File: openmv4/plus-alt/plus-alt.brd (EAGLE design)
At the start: 35.6 x 44.5 mm, 80 parts, among them M1 9774030243R, M2 9774030243R, Q1 BSS138, Q2 AO3401, U1 W25Q256JVEIQ_TR, U2 *, U3 ME6211C33M5G, U4 PAM2305AABADJ, U5 USBLC6-2, X1 MF-CON-MICROUSB-RIGHT, X2 USD-1040310811, X3 DF12-36-DS, X4 S2B-PH-K-S(LF)(SN), Y1 12M

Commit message: PureEngineering Updates
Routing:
- net VCC: track 125.5 -> 127.7 mm
- net VBUS: track 37.8 -> 39.8 mm
- net N$17: track 22.3 -> 23.7 mm
- net SPI2_NSS: track 16.7 -> 15.9 mm
- added copper zone on layer 5, net VCC
- removed copper zone on layer 16, net VBUS
- removed copper zone on layer 15, net VCC
- removed copper zone on layer 16, net VCC
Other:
- outline, holes or cut-outs redrawn

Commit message: Signals must be redone
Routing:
- net GND: track 136.2 -> 0.00 mm, vias 77 -> 0
- net VCC: track 127.7 -> 0.00 mm, vias 48 -> 0
- net SPI3_SCLK/TRACESWO: track 40.2 -> 0.00 mm, vias 3 -> 0
- net VBUS: track 39.8 -> 0.00 mm, vias 9 -> 0
- net SDIO_D0: track 36.9 -> 0.00 mm, vias 3 -> 0
- net DCMI_FSIN: track 36.8 -> 0.00 mm, vias 2 -> 0
- net DRAM_CLKE: track 35.2 -> 0.00 mm, vias 2 -> 0
- net DAC: track 34.6 -> 0.00 mm, vias 1 -> 0
- net SDIO_D1: track 34.3 -> 0.00 mm, vias 3 -> 0
- net TIM4_CH1: track 33.8 -> 0.00 mm, vias 1 -> 0
- net DRAM_DQM1: track 33.6 -> 0.00 mm, vias 1 -> 0
- net DRAM_D29: track 32.5 -> 0.00 mm, vias 2 -> 0
- net DCMI_RST: track 32.4 -> 0.00 mm, vias 4 -> 0
- net DRAM_D28: track 32.3 -> 0.00 mm, vias 2 -> 0
- net I2C1_SCL: track 31.6 -> 0.00 mm, vias 3 -> 0
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
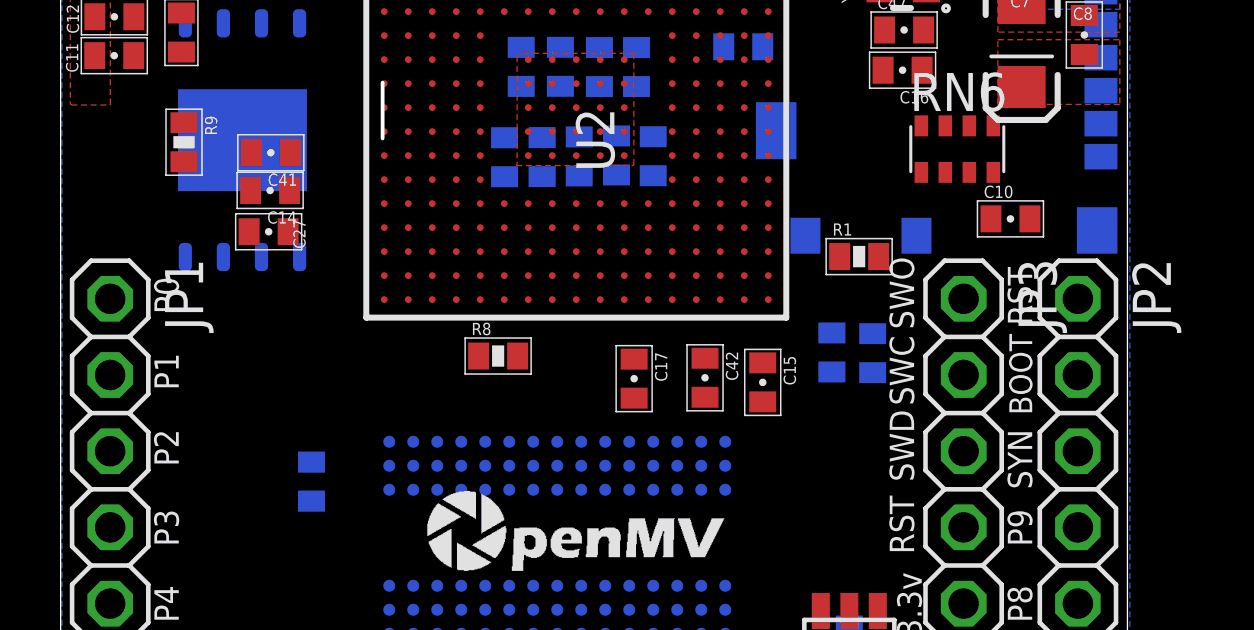
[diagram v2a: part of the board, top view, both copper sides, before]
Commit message: Fixed QSPI pins
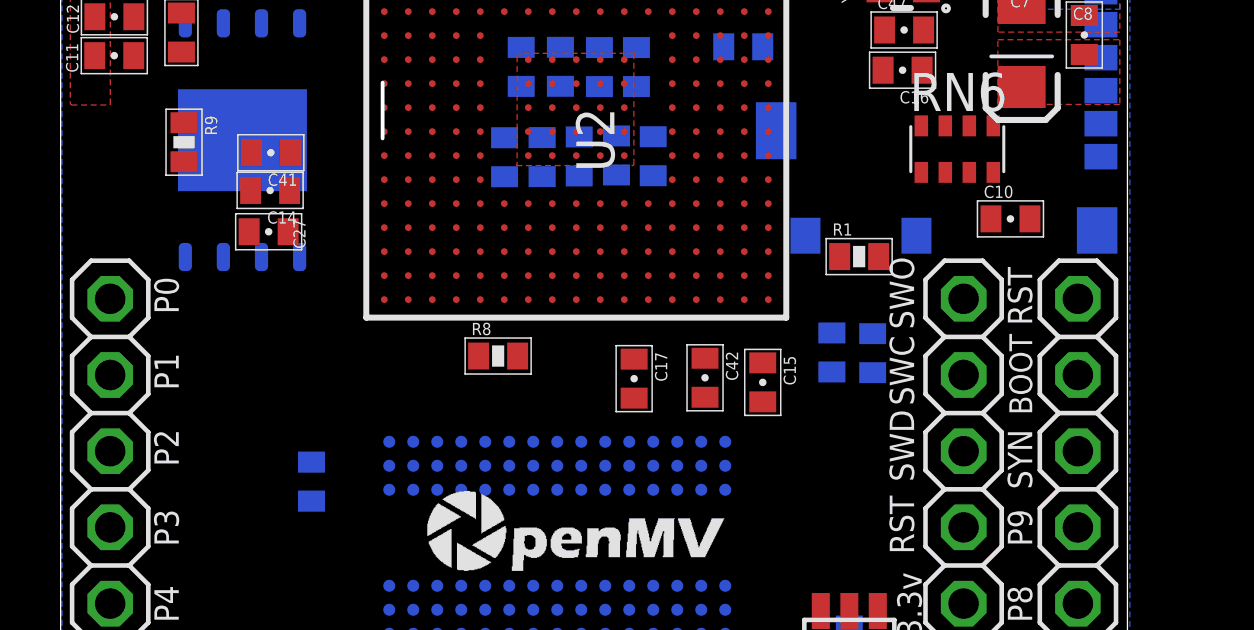
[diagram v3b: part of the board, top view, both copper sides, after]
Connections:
- net FLASH_IO0: now also U2.K4; no longer U2.L4
- net FLASH_IO1: now also U2.L4; no longer U2.K4
